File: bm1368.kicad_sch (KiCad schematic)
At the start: 57 parts, among them U1 25MHz, U2 TXB0104RGYR, U4 BM1368_mode1, U5 MCP1824T-1802E, U6 MCP1824T-0802E

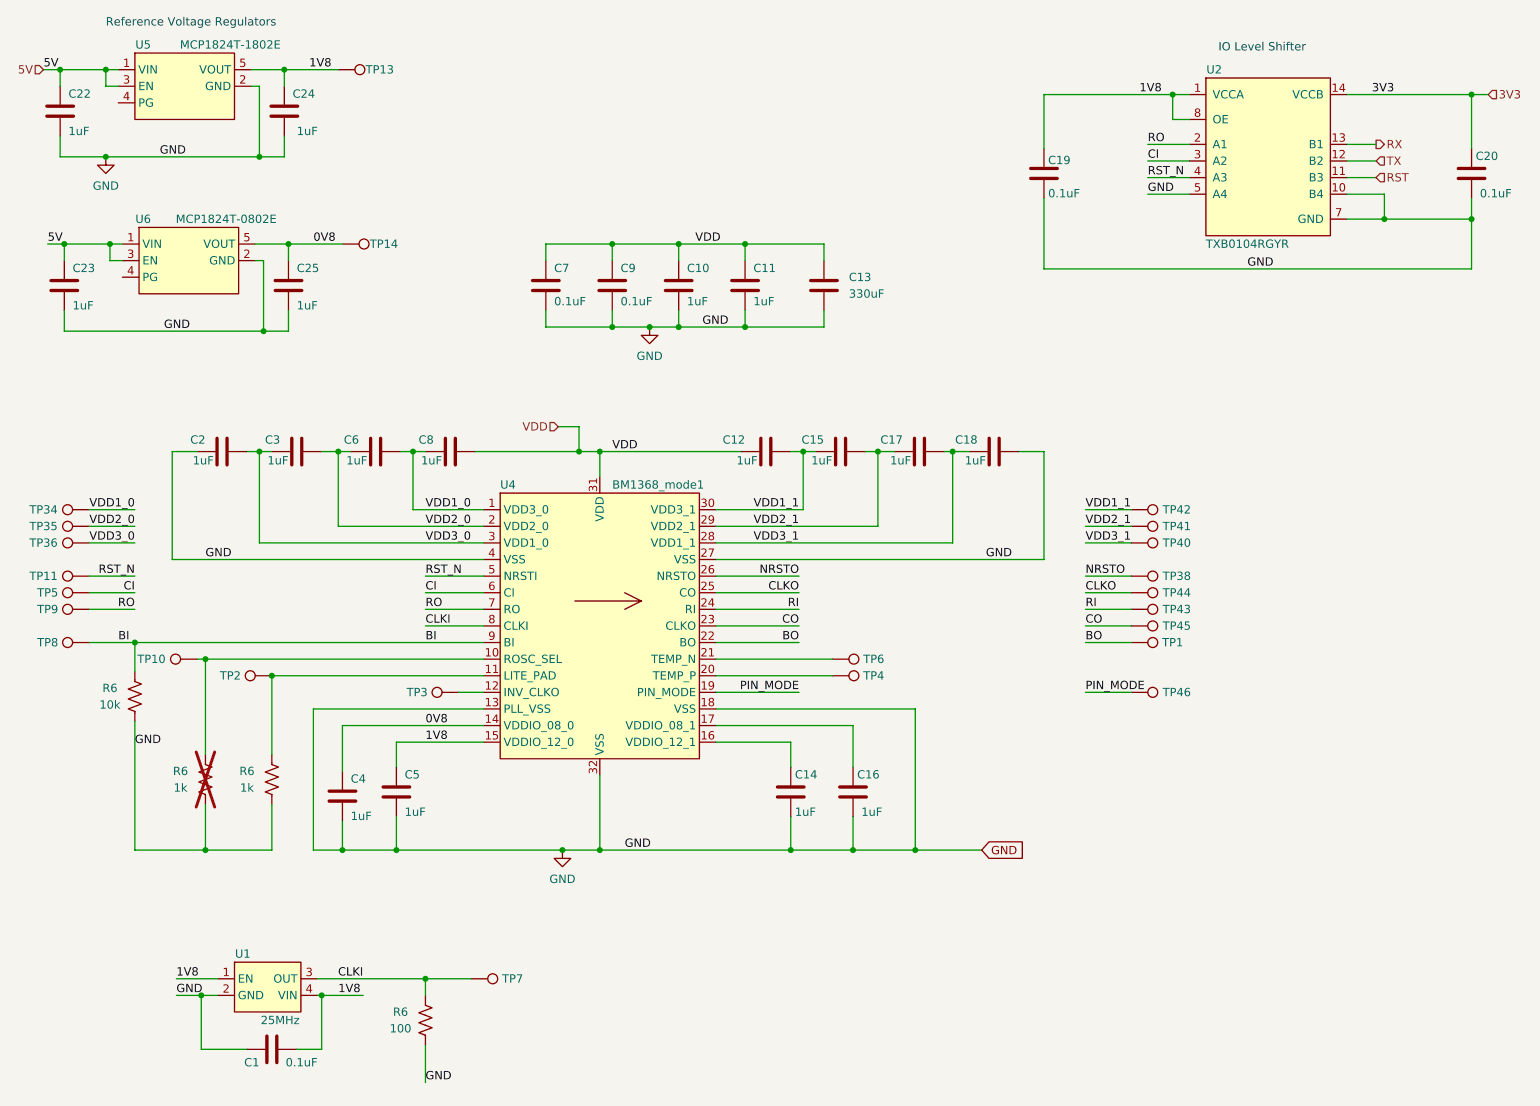
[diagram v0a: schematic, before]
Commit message: hooked up TEMP_P and TEMP_N. bumped version everywhere to 402
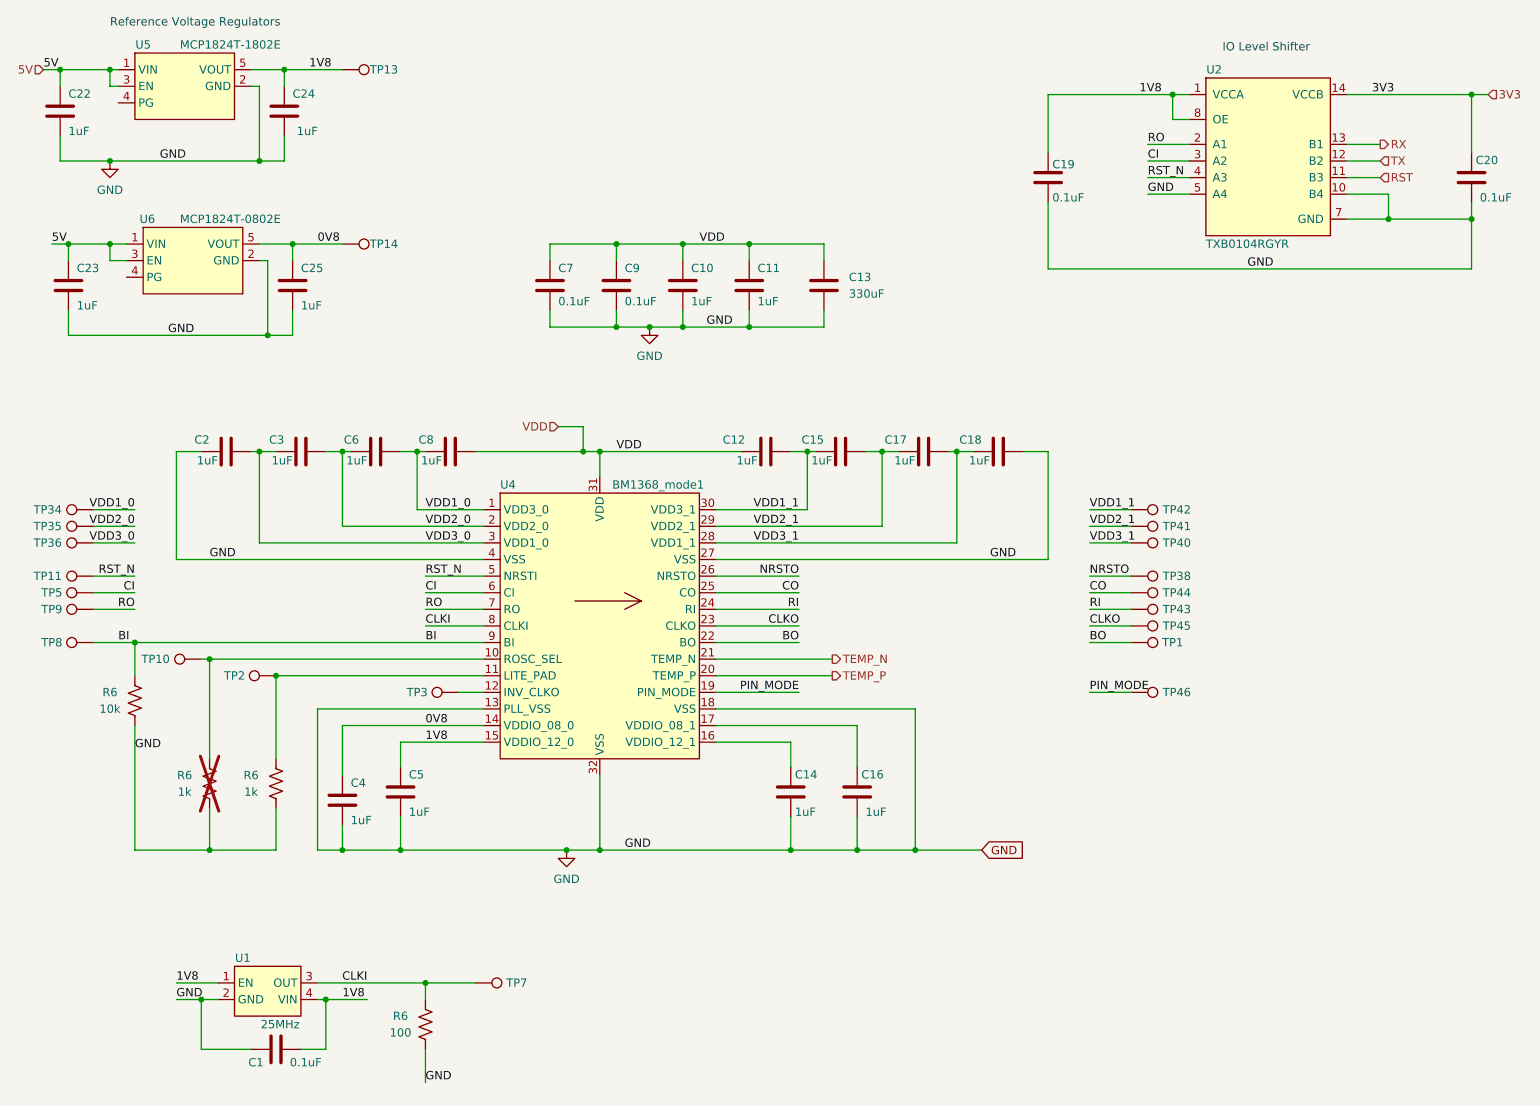
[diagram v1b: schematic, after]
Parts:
- removed TP4, TP6: TestPoint, TestPoint:TestPoint_Pad_D1.5mm, symbol Connector:TestPoint
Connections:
- net CLKO: now also TP45.1, U4.23 (CLKO); no longer TP44.1, U4.25 (CO)
- net CO: now also TP44.1, U4.25 (CO); no longer TP45.1, U4.23 (CLKO)
- net TEMP_N: now reaches U4.21 (TEMP_N)
- net TEMP_P: now reaches U4.20 (TEMP_P)
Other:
- moved on the sheet: C1, C10, C11, C16, C17, C18, C19, C2, C20, C23, C25, C3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

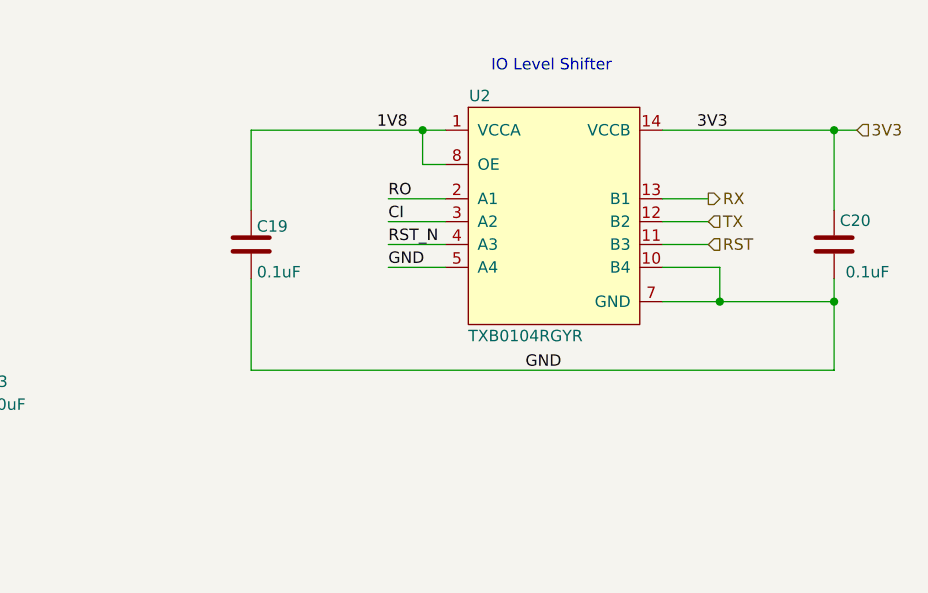
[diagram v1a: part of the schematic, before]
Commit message: changed fan capacitor to 100uF ceramic. Switched level shifter to SN74AVC4T774 for #146
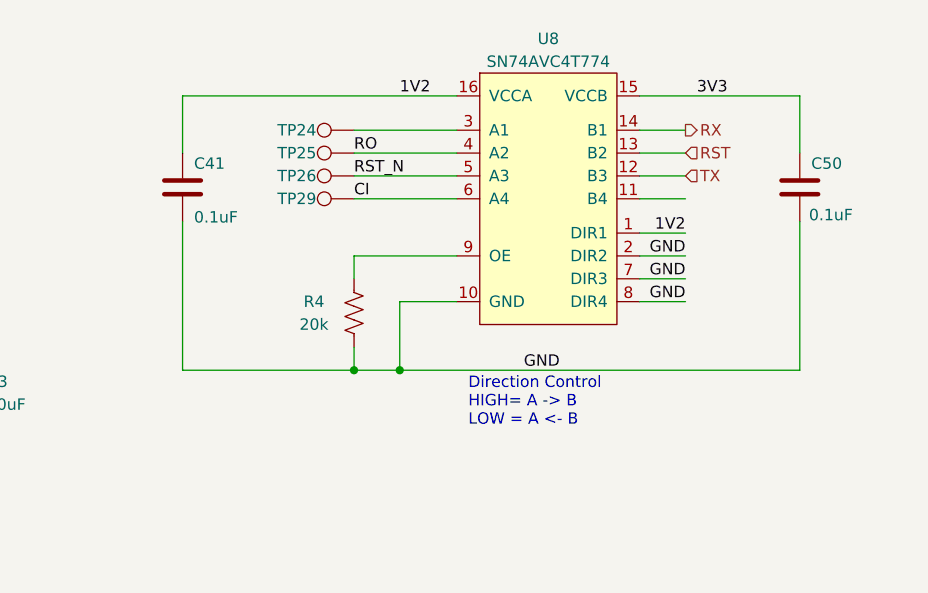
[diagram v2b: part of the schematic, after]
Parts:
- removed C19, C20: 0.1uF, Capacitor_SMD:C_0402_1005Metric, symbol Device:C
- removed U2: TXB0104RGYR, bitaxe:TXB0104, symbol bitaxe:TXB0104RGYR
- added C41, C50: 0.1uF, Capacitor_SMD:C_0402_1005Metric, symbol Device:C
- added R4: 20k, Resistor_SMD:R_0402_1005Metric, symbol Device:R_US
- added TP24, TP25, TP26, TP29: TestPoint, TestPoint:TestPoint_Pad_D1.0mm, symbol Connector:TestPoint
- added U8: SN74AVC4T774, Package_SO:TSSOP-16_4.4x5mm_P0.65mm, symbol bitaxe:SN74AVC4T774
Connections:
- net 3V3: now also C50.1, U8.15 (VCCB)
- net CI: now also TP29.1, U8.6 (A4)
- net GND: now also C41.2, C50.2, R4.1, U8.10 (GND), U8.2 (DIR2), U8.7 (DIR3), U8.8 (DIR4)
- net RO: now also TP25.1, U8.4 (A2)
- net RST: now also U8.13 (B2)
- net RST_N: now also TP26.1, U8.5 (A3)
- net RX: now also U8.14 (B1)
- net TX: now also U8.12 (B3)
- new net: R4.2, U8.9 (OE)
- new net: TP24.1, U8.3 (A1)
- new net 1V2: C41.1, U8.1 (DIR1), U8.16 (VCCA)
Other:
- note added: "Direction Control HIGH= A -> B LOW = A <- B"
- note removed: "IO Level Shifter"

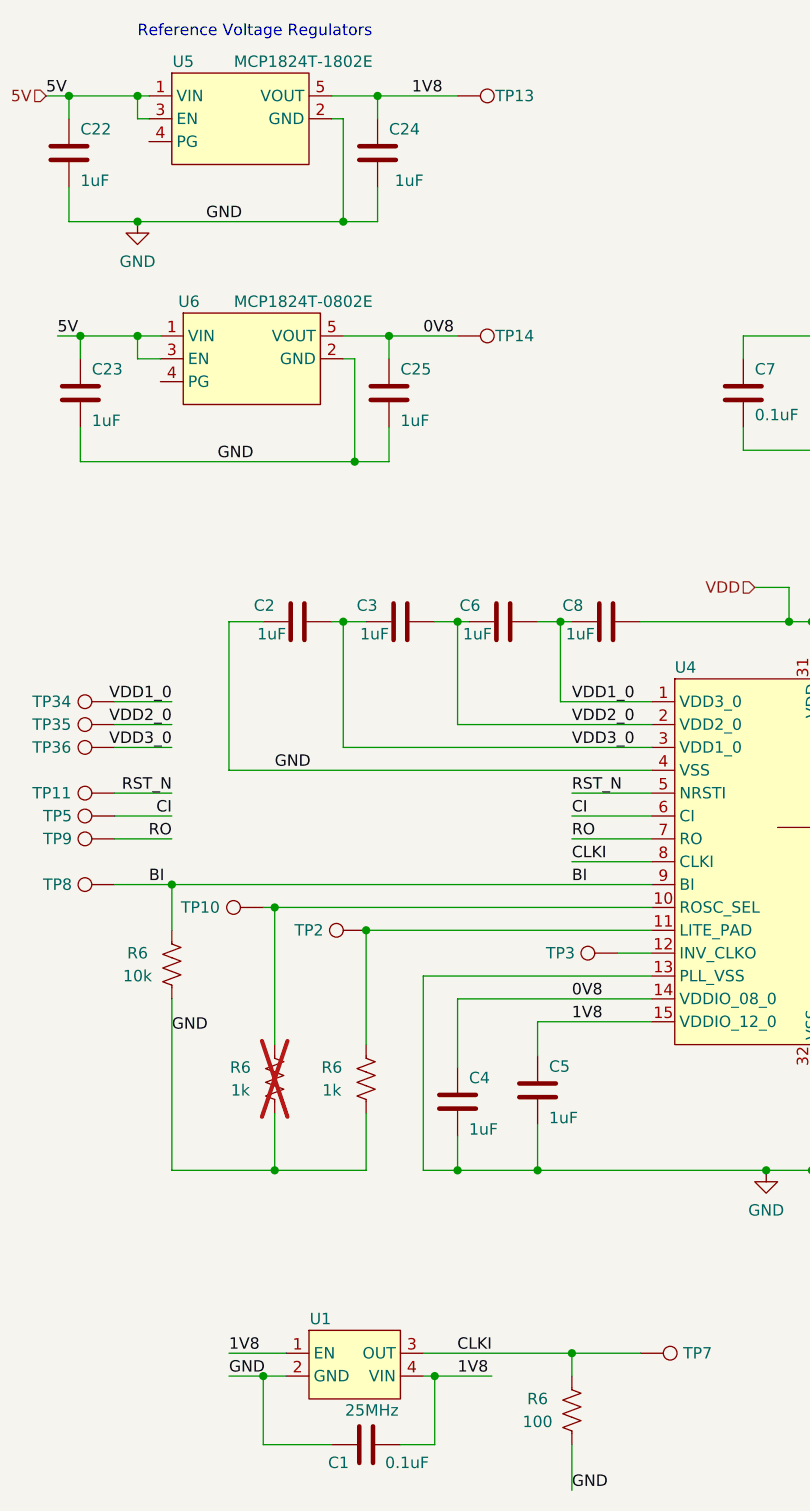
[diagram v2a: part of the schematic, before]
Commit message: changed 1.8V LDO to 1.2V LDO and 25MHz OSC to 1.2V model for #63
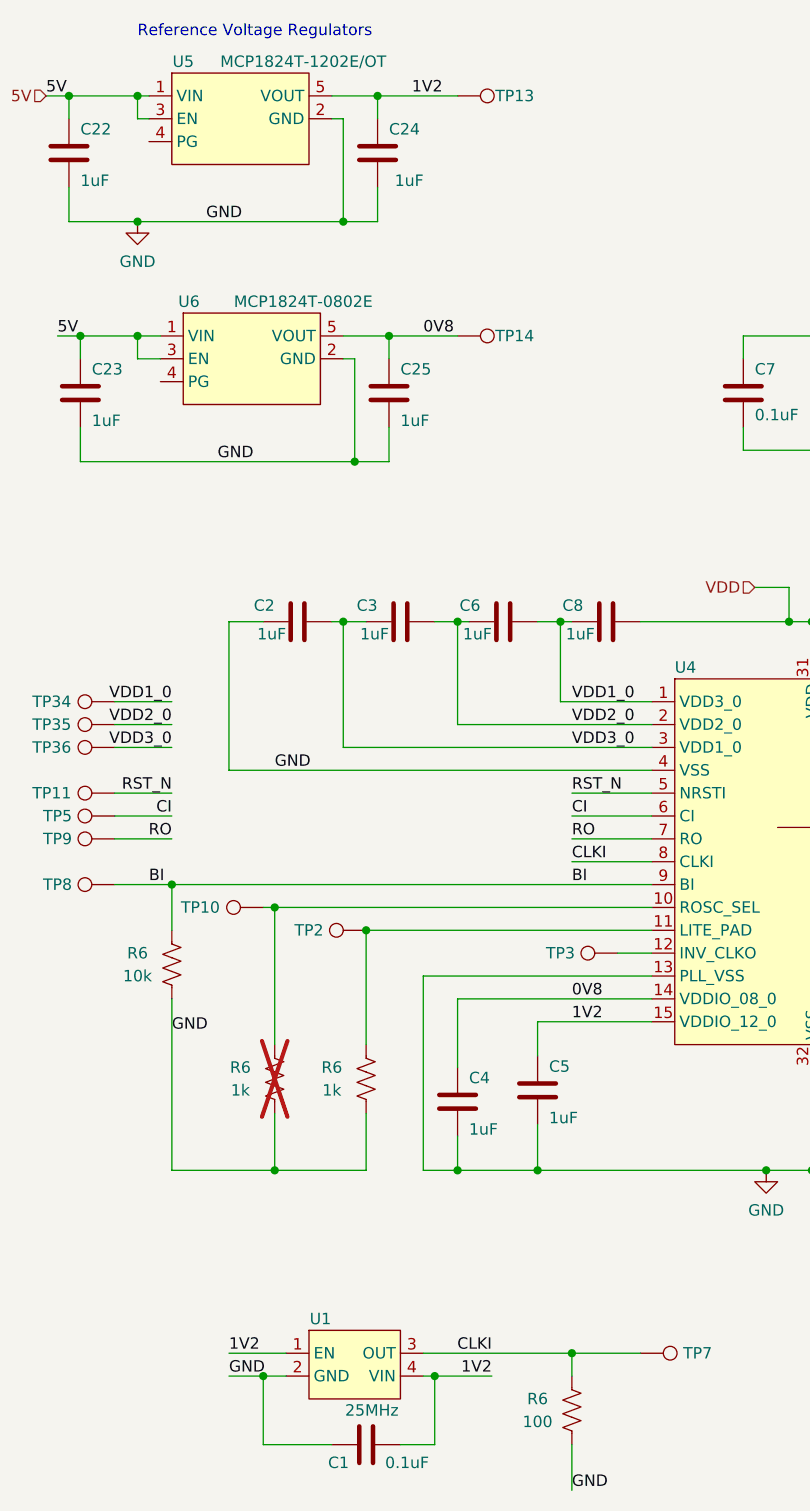
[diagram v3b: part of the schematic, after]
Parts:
- U1: DK 1908-O250-JO32-B-1V3-1-T1-LFCT-ND -> (none); LCSC (none) -> C5137262; PARTNO O 25,0-JO32-B-1V3-1-T1-LF -> SX3M25.000E20F30THN
- U5: value MCP1824T-1802E -> MCP1824T-1202E/OT; DK MCP1824T-1802E/OTCT-ND -> MCP1824T-1202E/OTCT-ND; PARTNO MCP1824T-1802E/OT -> MCP1824T-1202E/OT
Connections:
- net 1V8 is gone; now on net 1V2: C1.2, C24.1, C5.1, TP13.1, U1.1 (EN), U1.4 (VIN), U4.15 (VDDIO_12_0), U5.5 (VOUT)
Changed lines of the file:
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@@
 		)
 	)
-	(label "1V8"
+	(label "1V2"
 		(at 86.36 132.08 0)
 		(fields_autoplaced yes)
@@
 		)
 	)
-	(label "1V8"
+	(label "1V2"
 		(at 68.58 29.21 0)
 		(fields_autoplaced yes)
@@
 		)
 	)
-	(label "1V8"
+	(label "1V2"
 		(at 48.26 168.91 0)
 		(fields_autoplaced yes)
@@
 		)
 	)
-	(label "1V8"
-		(at 73.66 171.45 0)
+	(label "1V2"
+		(at 77.47 171.45 180)
 		(fields_autoplaced yes)
 		(effects
@@
 				(size 1.27 1.27)
 			)
-			(justify left bottom)
+			(justify right bottom)
 		)
 	)
@@
 			)
 		)
-		(property "Datasheet" "https://www.jauch.com/downloadfile/5ef1edcfb8e2f73163c8ce8009ef659d1/jo32-1.8-3.3v.pdf"
+		(property "Datasheet" ""
 			(at 60.96 171.45 0)
 			(effects
@@
 			)
 		)
-		(property "DK" "1908-O250-JO32-B-1V3-1-T1-LFCT-ND"
+		(property "DK" ""
+			(at 62.23 170.18 0)
+			(effects
+				(font
+					(size 1.27 1.27)
+				)
+				(hide yes)
+			)
+		)
+		(property "PARTNO" "SX3M25.000E20F30THN"
 			(at 62.23 170.18 0)
 			(effects
@@
 			)
 		)
-		(property "PARTNO" "O 25,0-JO32-B-1V3-1-T1-LF"
+		(property "LCSC" "C5137262"
 			(at 62.23 170.18 0)
 			(effects
@@
 			)
 		)
-		(property "Value" "MCP1824T-1802E"
+		(property "Value" "MCP1824T-1202E/OT"
 			(at 56.515 25.4 0)
 			(effects
@@
 			)
 		)
-		(property "PARTNO" "MCP1824T-1802E/OT"
+		(property "PARTNO" "MCP1824T-1202E/OT"
 			(at 49.53 30.48 0)
 			(effects
@@
 			)
 		)
-		(property "DK" "MCP1824T-1802E/OTCT-ND"
+		(property "DK" "MCP1824T-1202E/OTCT-ND"
 			(at 49.53 30.48 0)
 			(effects

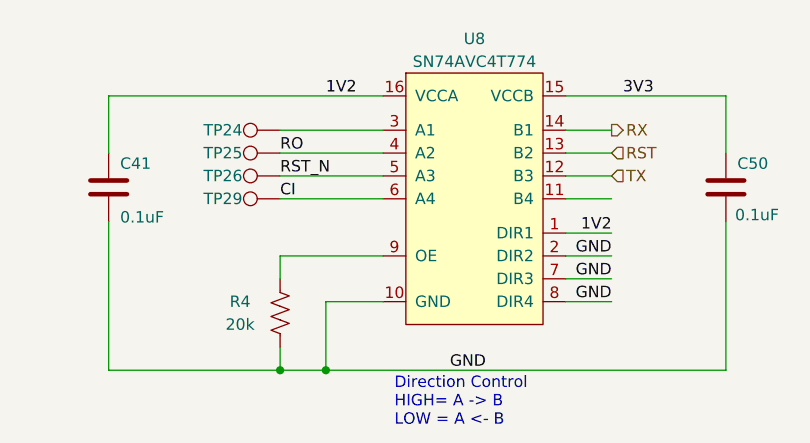
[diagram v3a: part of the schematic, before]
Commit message: started placing TPS546D24A
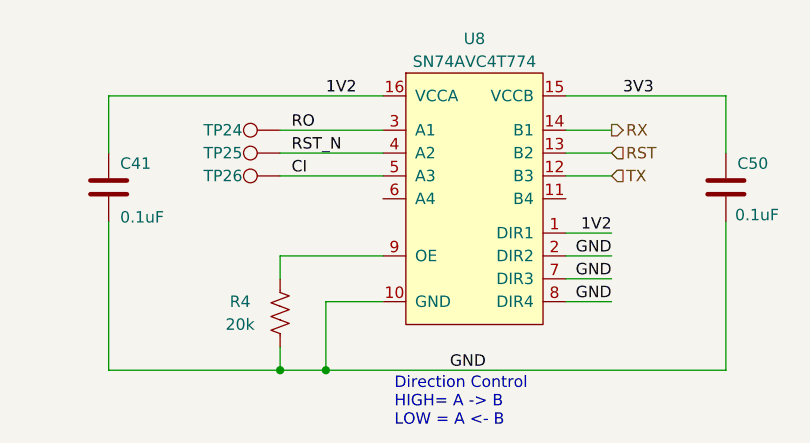
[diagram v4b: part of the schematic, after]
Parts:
- removed TP29: TestPoint, TestPoint:TestPoint_Pad_D1.0mm, symbol Connector:TestPoint
- TP24, TP25, TP26: footprint TestPoint:TestPoint_Pad_D1.0mm -> TestPoint:TestPoint_Pad_D1.5mm
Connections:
- net CI: now also TP26.1, U8.5 (A3); no longer U8.6 (A4)
- net RO: now also TP24.1, U8.3 (A1); no longer TP25.1, U8.4 (A2)
- net RST_N: now also TP25.1, U8.4 (A2); no longer TP26.1, U8.5 (A3)
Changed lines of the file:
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@@
 	(wire
 		(pts
-			(xy 193.04 40.64) (xy 204.47 40.64)
-		)
-		(stroke
-			(width 0)
-			(type default)
-		)
-	)
-	(wire
-		(pts
 			(xy 31.75 55.88) (xy 31.75 58.42)
 		)
@@
 	(wire
 		(pts
-			(xy 224.79 40.64) (xy 229.87 40.64)
-		)
-		(stroke
-			(width 0)
-			(type default)
-		)
-	)
-	(wire
-		(pts
 			(xy 187.96 114.3) (xy 194.31 114.3)
 		)
@@
 	)
 	(label "CI"
-		(at 193.04 40.64 0)
+		(at 194.31 38.1 0)
 		(fields_autoplaced yes)
 		(effects
@@
 	)
 	(label "RO"
-		(at 193.04 35.56 0)
+		(at 194.31 33.02 0)
 		(fields_autoplaced yes)
 		(effects
@@
 	)
 	(label "RST_N"
-		(at 193.04 38.1 0)
+		(at 194.31 35.56 0)
 		(fields_autoplaced yes)
 		(effects
@@
 			)
 		)
-		(property "Footprint" "TestPoint:TestPoint_Pad_D1.0mm"
+		(property "Footprint" "TestPoint:TestPoint_Pad_D1.5mm"
 			(at 193.04 33.02 0)
 			(effects
@@
 			)
 		)
-		(property "Footprint" "TestPoint:TestPoint_Pad_D1.0mm"
+		(property "Footprint" "TestPoint:TestPoint_Pad_D1.5mm"
 			(at 193.04 27.94 0)
 			(effects
@@
 			)
 		)
-		(property "Footprint" "TestPoint:TestPoint_Pad_D1.0mm"
+		(property "Footprint" "TestPoint:TestPoint_Pad_D1.5mm"
 			(at 193.04 30.48 0)
 			(effects
@@
 					(unit 1)
 				)
-			)
-		)
-	)
-	(symbol
-		(lib_id "Connector:TestPoint")
-		(at 193.04 40.64 90)
-		(unit 1)
-		(exclude_from_sim no)
-		(in_bom no)
-		(on_board yes)
-		(dnp no)
-		(property "Reference" "TP29"
-			(at 186.69 40.64 90)
-			(effects
-				(font
-					(size 1.27 1.27)
-				)
-			)
-		)
-		(property "Value" "TestPoint"
-			(at 187.325 39.3701 90)
-			(effects
-				(font
-					(size 1.27 1.27)
-				)
-				(justify left)
-				(hide yes)
-			)
-		)
-		(property "Footprint" "TestPoint:TestPoint_Pad_D1.0mm"
-			(at 193.04 35.56 0)
-			(effects
-				(font
-					(size 1.27 1.27)
-				)
-				(hide yes)
-			)
-		)
-		(property "Datasheet" "~"
-			(at 193.04 35.56 0)
-			(effects
-				(font
-					(size 1.27 1.27)
-				)
-				(hide yes)
-			)
-		)
-		(property "Description" ""
-			(at 193.04 40.64 0)
-			(effects
-				(font
-					(size 1.27 1.27)
-				)
-				(hide yes)
-			)
-		)
-		(pin "1"
-		)
-		(instances
-			(project "bitaxeSupra"
-				(path "/e63e39d7-6ac0-4ffd-8aa3-1841a4541b55/4cf9c075-d009-4c35-9949-adda70ae20c7"
-					(reference "TP29")
-					(unit 1)
-				)
